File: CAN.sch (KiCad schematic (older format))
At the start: 7 parts, among them IC1 ADM3052

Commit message: - updated project to 5.0.0 - added ignore file
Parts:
- C10, C11, C12, C9: symbol C_Small -> Device:C_Small
- IC1: symbol ADM3052 -> HSWR-V2-rescue:ADM3052
- R30, R31: symbol R_Small -> Device:R_Small
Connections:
- wire segments 4 -> 2
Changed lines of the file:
@@
-EESchema Schematic File Version 2
-LIBS:HSWR V2-rescue
-LIBS:power
-LIBS:device
-LIBS:transistors
-LIBS:conn
-LIBS:linear
-LIBS:regul
-LIBS:74xx
-LIBS:cmos4000
-LIBS:adc-dac
-LIBS:memory
-LIBS:xilinx
-LIBS:microcontrollers
-LIBS:dsp
-LIBS:microchip
-LIBS:analog_switches
-LIBS:motorola
-LIBS:texas
-LIBS:intel
-LIBS:audio
-LIBS:interface
-LIBS:digital-audio
-LIBS:philips
-LIBS:display
-LIBS:cypress
-LIBS:siliconi
-LIBS:opto
-LIBS:atmel
-LIBS:contrib
-LIBS:valves
+EESchema Schematic File Version 4
 LIBS:HSWR V2-cache
-EELAYER 25 0
+EELAYER 26 0
 EELAYER END
 $Descr A4 11693 8268
@@
 CANL
 $Comp
-L ADM3052 IC1
+L HSWR-V2-rescue:ADM3052 IC1
 U 1 1 5759CEA3
 P 6000 3850
+AR Path="/5759CEA3" Ref="IC1"  Part="1"
+AR Path="/5899E225/5759CEA3" Ref="IC1"  Part="1"
 F 0 "IC1" H 6000 3850 60  0000 C CNN
 F 1 "ADM3052" H 6000 4500 60  0000 C CNN
@@
 $EndComp
 $Comp
-L C_Small C9
+L Device:C_Small C9
 U 1 1 5759CF39
 P 5350 3900
@@
 $EndComp
 $Comp
-L C_Small C10
+L Device:C_Small C10
 U 1 1 5759CF9E
 P 5350 4200
@@
 Connection ~ 5350 4300
 $Comp
-L R_Small R31
+L Device:R_Small R31
 U 1 1 5759CFE0
 P 5350 4400
@@
 $EndComp
 $Comp
-L C_Small C11
+L Device:C_Small C11
 U 1 1 5759D08A
 P 5350 4600
@@
 Connection ~ 5350 4500
 $Comp
-L Earth #PWR029
+L power:Earth #PWR029
 U 1 1 5759DCFE
 P 5350 4700
@@
 $EndComp
 $Comp
-L Earth #PWR030
+L power:Earth #PWR030
 U 1 1 5759DF52
 P 5350 4100
@@
 $EndComp
 $Comp
-L +12VA #PWR031
+L power:+12VA #PWR031
 U 1 1 5759E22F
 P 5350 4500
@@
 $EndComp
 $Comp
-L GND #PWR032
+L power:GND #PWR032
 U 1 1 5759E8F5
 P 6650 4500
@@
 $EndComp
 $Comp
-L R_Small R30
+L Device:R_Small R30
 U 1 1 5759ED7A
 P 5350 3250
@@
 V+Sense
 $Comp
-L C_Small C12
+L Device:C_Small C12
 U 1 1 575A0498
 P 6650 4200
@@
 Connection ~ 6650 4500
 $Comp
-L +3V3 #PWR033
+L power:+3V3 #PWR033
 U 1 1 575A0BC8
 P 6650 4100
@@
 	1    0    0    -1
 $EndComp
-Wire Wire Line
-	6650 4300 6650 4500
 Connection ~ 6650 4400
-Wire Wire Line
-	5350 4000 5350 4100
 Connection ~ 5350 4000
 Connection ~ 6650 4100

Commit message: - updated to VESC6 architecture - still some things to do in schematic
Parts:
- removed IC1: ADM3052, Housings_SOIC:SOIC-16_7.5x10.3mm_Pitch1.27mm, symbol HSWR-V2-rescue:ADM3052
- C10, C11, C12, C9: footprint Capacitors_SMD:C_0805 -> Capacitor_SMD:C_0805_2012Metric
- R30: footprint Resistors_SMD:R_0805 -> Resistor_SMD:R_0805_2012Metric
- R31: footprint Resistors_SMD:R_1206 -> Resistor_SMD:R_0805_2012Metric
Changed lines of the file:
@@
 $Descr A4 11693 8268
 encoding utf-8
-Sheet 3 7
+Sheet 2 7
 Title "HSWR CAN Transceiver"
 Date "2017-02-05"
@@
 CANL
 $Comp
-L HSWR-V2-rescue:ADM3052 IC1
-U 1 1 5759CEA3
-P 6000 3850
-AR Path="/5759CEA3" Ref="IC1"  Part="1"
-AR Path="/5899E225/5759CEA3" Ref="IC1"  Part="1"
-F 0 "IC1" H 6000 3850 60  0000 C CNN
-F 1 "ADM3052" H 6000 4500 60  0000 C CNN
-F 2 "Housings_SOIC:SOIC-16_7.5x10.3mm_Pitch1.27mm" H 6150 3950 60  0001 C CNN
-F 3 "" H 6150 3950 60  0000 C CNN
-	1    6000 3850
-	-1   0    0    -1
-$EndComp
-$Comp
 L Device:C_Small C9
 U 1 1 5759CF39
@@
 F 0 "C9" H 5500 4000 50  0000 L CNN
 F 1 "1u" H 5500 3900 50  0000 L CNN
-F 2 "Capacitors_SMD:C_0805" H 5350 3900 60  0001 C CNN
+F 2 "Capacitor_SMD:C_0805_2012Metric" H 5350 3900 60  0001 C CNN
 F 3 "" H 5350 3900 60  0000 C CNN
 	1    5350 3900
@@
 F 0 "C10" H 5450 4250 50  0000 L CNN
 F 1 "10u" H 5450 4150 50  0000 L CNN
-F 2 "Capacitors_SMD:C_0805" H 5350 4200 60  0001 C CNN
+F 2 "Capacitor_SMD:C_0805_2012Metric" H 5350 4200 60  0001 C CNN
 F 3 "" H 5350 4200 60  0000 C CNN
 	1    5350 4200
 	-1   0    0    -1
 $EndComp
-Connection ~ 5350 4100
-Connection ~ 5350 4300
 $Comp
 L Device:R_Small R31
@@
 F 0 "R31" V 5250 4350 50  0000 L CNN
 F 1 "300R" H 5400 4400 50  0000 L CNN
-F 2 "Resistors_SMD:R_1206" H 5350 4400 60  0001 C CNN
+F 2 "Resistor_SMD:R_0805_2012Metric" H 5350 4400 60  0001 C CNN
 F 3 "" H 5350 4400 60  0000 C CNN
 	1    5350 4400
@@
 F 0 "C11" H 5500 4600 50  0000 L CNN
 F 1 "100n" H 5450 4500 50  0000 L CNN
-F 2 "Capacitors_SMD:C_0805" H 5350 4600 60  0001 C CNN
+F 2 "Capacitor_SMD:C_0805_2012Metric" H 5350 4600 60  0001 C CNN
 F 3 "" H 5350 4600 60  0000 C CNN
 	1    5350 4600
@@
 F 0 "R30" V 5250 3200 50  0000 L CNN
 F 1 "120R" H 5400 3250 50  0000 L CNN
-F 2 "Resistors_SMD:R_0805" H 5350 3250 60  0001 C CNN
+F 2 "Resistor_SMD:R_0805_2012Metric" H 5350 3250 60  0001 C CNN
 F 3 "" H 5350 3250 60  0000 C CNN
 	1    5350 3250
@@
 Wire Wire Line
 	5350 3150 5150 3150
-Connection ~ 5350 3150
-Connection ~ 5350 3350
 Text HLabel 6650 3550 2    60   Output ~ 0
 V+Sense
@@
 F 0 "C12" H 6800 4200 50  0000 L CNN
 F 1 "100n" H 6750 4100 50  0000 L CNN
-F 2 "Capacitors_SMD:C_0805" H 6650 4200 60  0001 C CNN
+F 2 "Capacitor_SMD:C_0805_2012Metric" H 6650 4200 60  0001 C CNN
 F 3 "" H 6650 4200 60  0000 C CNN
 	1    6650 4200
 	1    0    0    -1
 $EndComp
-Connection ~ 6650 4300
-Connection ~ 6650 4500
 $Comp
 L power:+3V3 #PWR033
@@
 	1    0    0    -1
 $EndComp
-Connection ~ 6650 4400
-Connection ~ 5350 4000
-Connection ~ 6650 4100
 $EndSCHEMATC

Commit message: - layout pretty much finished except PSU and maaaaybe R2D - started work on R2D with AD2S1205
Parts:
- removed C10: 10u, Capacitor_SMD:C_0805_2012Metric, symbol Device:C_Small
- removed R31: 300R, Resistor_SMD:R_0805_2012Metric, symbol Device:R_Small
- added IC4: ADUM3054, Package_SO:SOIC-16W_7.5x10.3mm_P1.27mm, symbol Auktoralib:ADUM3054
- added U5: AP1117-50, Package_TO_SOT_SMD:SOT-223-3_TabPin2, symbol Regulator_Linear:AP1117-50
- C9: value 1u -> 100n
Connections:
- net labels added: 12V_ext
- net labels removed: +12VA
- wire segments 2 -> 8
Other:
- moved on the sheet: C11, C12, C9
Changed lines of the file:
@@
 $Descr A4 11693 8268
 encoding utf-8
-Sheet 2 7
+Sheet 7 9
 Title "HSWR CAN Transceiver"
 Date "2017-02-05"
@@
 Comment4 ""
 $EndDescr
-Text HLabel 6650 3350 2    60   Output ~ 0
+Text HLabel 6550 3400 2    60   Output ~ 0
 CAN_RX
-Text HLabel 6650 3150 2    60   Input ~ 0
+Text HLabel 6550 3500 2    60   Input ~ 0
 CAN_TX
 Text HLabel 5150 3150 0    60   Input ~ 0
@@
 L Device:C_Small C9
 U 1 1 5759CF39
-P 5350 3900
-F 0 "C9" H 5500 4000 50  0000 L CNN
-F 1 "1u" H 5500 3900 50  0000 L CNN
-F 2 "Capacitor_SMD:C_0805_2012Metric" H 5350 3900 60  0001 C CNN
-F 3 "" H 5350 3900 60  0000 C CNN
-	1    5350 3900
-	-1   0    0    -1
-$EndComp
-$Comp
-L Device:C_Small C10
-U 1 1 5759CF9E
-P 5350 4200
-F 0 "C10" H 5450 4250 50  0000 L CNN
-F 1 "10u" H 5450 4150 50  0000 L CNN
-F 2 "Capacitor_SMD:C_0805_2012Metric" H 5350 4200 60  0001 C CNN
-F 3 "" H 5350 4200 60  0000 C CNN
-	1    5350 4200
-	-1   0    0    -1
-$EndComp
-$Comp
-L Device:R_Small R31
-U 1 1 5759CFE0
-P 5350 4400
-F 0 "R31" V 5250 4350 50  0000 L CNN
-F 1 "300R" H 5400 4400 50  0000 L CNN
-F 2 "Resistor_SMD:R_0805_2012Metric" H 5350 4400 60  0001 C CNN
-F 3 "" H 5350 4400 60  0000 C CNN
-	1    5350 4400
+P 5700 2600
+F 0 "C9" H 5800 2600 50  0000 L CNN
+F 1 "100n" H 5750 2500 50  0000 L CNN
+F 2 "Capacitor_SMD:C_0805_2012Metric" H 5700 2600 60  0001 C CNN
+F 3 "" H 5700 2600 60  0000 C CNN
+	1    5700 2600
 	-1   0    0    -1
 $EndComp
@@
 L Device:C_Small C11
 U 1 1 5759D08A
-P 5350 4600
-F 0 "C11" H 5500 4600 50  0000 L CNN
-F 1 "100n" H 5450 4500 50  0000 L CNN
-F 2 "Capacitor_SMD:C_0805_2012Metric" H 5350 4600 60  0001 C CNN
-F 3 "" H 5350 4600 60  0000 C CNN
-	1    5350 4600
-	-1   0    0    -1
-$EndComp
-Connection ~ 5350 4500
+P 4350 2600
+F 0 "C11" H 4500 2600 50  0000 L CNN
+F 1 "100n" H 4450 2500 50  0000 L CNN
+F 2 "Capacitor_SMD:C_0805_2012Metric" H 4350 2600 60  0001 C CNN
+F 3 "" H 4350 2600 60  0000 C CNN
+	1    4350 2600
+	-1   0    0    -1
+$EndComp
 $Comp
 L power:Earth #PWR029
 U 1 1 5759DCFE
-P 5350 4700
-F 0 "#PWR029" H 5350 4450 50  0001 C CNN
-F 1 "Earth" H 5350 4550 50  0001 C CNN
-F 2 "" H 5350 4700 60  0000 C CNN
-F 3 "" H 5350 4700 60  0000 C CNN
-	1    5350 4700
-	-1   0    0    -1
-$EndComp
-$Comp
-L power:Earth #PWR030
-U 1 1 5759DF52
-P 5350 4100
-F 0 "#PWR030" H 5350 3850 50  0001 C CNN
-F 1 "Earth" H 5350 3950 50  0001 C CNN
-F 2 "" H 5350 4100 60  0000 C CNN
-F 3 "" H 5350 4100 60  0000 C CNN
-	1    5350 4100
-	0    1    -1   0
-$EndComp
-$Comp
-L power:+12VA #PWR031
-U 1 1 5759E22F
-P 5350 4500
-F 0 "#PWR031" H 5350 4350 50  0001 C CNN
-F 1 "+12VA" V 5350 4750 50  0000 C CNN
-F 2 "" H 5350 4500 60  0000 C CNN
-F 3 "" H 5350 4500 60  0000 C CNN
-	1    5350 4500
-	0    -1   -1   0
+P 4650 2800
+F 0 "#PWR029" H 4650 2550 50  0001 C CNN
+F 1 "Earth" H 4650 2650 50  0001 C CNN
+F 2 "" H 4650 2800 60  0000 C CNN
+F 3 "" H 4650 2800 60  0000 C CNN
+	1    4650 2800
+	-1   0    0    -1
 $EndComp
 $Comp
 L power:GND #PWR032
 U 1 1 5759E8F5
-P 6650 4500
-F 0 "#PWR032" H 6650 4250 50  0001 C CNN
-F 1 "GND" H 6650 4350 50  0000 C CNN
-F 2 "" H 6650 4500 60  0000 C CNN
-F 3 "" H 6650 4500 60  0000 C CNN
-	1    6650 4500
+P 6050 4050
+F 0 "#PWR032" H 6050 3800 50  0001 C CNN
+F 1 "GND" H 6050 3900 50  0000 C CNN
+F 2 "" H 6050 4050 60  0000 C CNN
+F 3 "" H 6050 4050 60  0000 C CNN
+	1    6050 4050
 	1    0    0    -1
 $EndComp
@@
 Wire Wire Line
 	5350 3150 5150 3150
-Text HLabel 6650 3550 2    60   Output ~ 0
+Text HLabel 6550 3300 2    60   Output ~ 0
 V+Sense
 $Comp
 L Device:C_Small C12
 U 1 1 575A0498
-P 6650 4200
-F 0 "C12" H 6800 4200 50  0000 L CNN
-F 1 "100n" H 6750 4100 50  0000 L CNN
-F 2 "Capacitor_SMD:C_0805_2012Metric" H 6650 4200 60  0001 C CNN
-F 3 "" H 6650 4200 60  0000 C CNN
-	1    6650 4200
+P 6200 2600
+F 0 "C12" H 6350 2600 50  0000 L CNN
+F 1 "100n" H 6300 2500 50  0000 L CNN
+F 2 "Capacitor_SMD:C_0805_2012Metric" H 6200 2600 60  0001 C CNN
+F 3 "" H 6200 2600 60  0000 C CNN
+	1    6200 2600
 	1    0    0    -1
 $EndComp
@@
 L power:+3V3 #PWR033
 U 1 1 575A0BC8
-P 6650 4100
-F 0 "#PWR033" H 6650 3950 50  0001 C CNN
-F 1 "+3V3" H 6650 4240 50  0000 C CNN
-F 2 "" H 6650 4100 60  0000 C CNN
-F 3 "" H 6650 4100 60  0000 C CNN
-	1    6650 4100
-	1    0    0    -1
-$EndComp
+P 6200 2500
+F 0 "#PWR033" H 6200 2350 50  0001 C CNN
+F 1 "+3V3" H 6200 2640 50  0000 C CNN
+F 2 "" H 6200 2500 60  0000 C CNN
+F 3 "" H 6200 2500 60  0000 C CNN
+	1    6200 2500
+	1    0    0    -1
+$EndComp
+$Comp
+L power:Earth #PWR0115
+U 1 1 5CA085F6
+P 5700 2700
+F 0 "#PWR0115" H 5700 2450 50  0001 C CNN
+F 1 "Earth" H 5700 2550 50  0001 C CNN
+F 2 "" H 5700 2700 60  0000 C CNN
+F 3 "" H 5700 2700 60  0000 C CNN
+	1    5700 2700
+	-1   0    0    -1
+$EndComp
+Text HLabel 4350 2500 0    50   Input ~ 0
+12V_ext
+$Comp
+L Regulator_Linear:AP1117-50 U5
+U 1 1 5CA08F00
+P 4650 2500
+F 0 "U5" H 4650 2742 50  0000 C CNN
+F 1 "AP1117-50" H 4650 2651 50  0000 C CNN
+F 2 "Package_TO_SOT_SMD:SOT-223-3_TabPin2" H 4650 2700 50  0001 C CNN
+F 3 "http://www.diodes.com/datasheets/AP1117.pdf" H 4750 2250 50  0001 C CNN
+	1    4650 2500
+	1    0    0    -1
+$EndComp
+$Comp
+L power:Earth #PWR0167
+U 1 1 5CA09500
+P 4350 2800
+F 0 "#PWR0167" H 4350 2550 50  0001 C CNN
+F 1 "Earth" H 4350 2650 50  0001 C CNN
+F 2 "" H 4350 2800 60  0000 C CNN
+F 3 "" H 4350 2800 60  0000 C CNN
+	1    4350 2800
+	-1   0    0    -1
+$EndComp
+Wire Wire Line
+	4350 2800 4350 2700
+Wire Wire Line
+	4950 2500 5700 2500
+Wire Wire Line
+	5850 2500 5850 2750
+Connection ~ 5700 2500
+Wire Wire Line
+	5700 2500 5850 2500
+Connection ~ 5350 3150
+Connection ~ 5350 3350
+$Comp
+L Auktoralib:ADUM3054 IC4
+U 1 1 5CA06D6C
+P 5950 3400
+F 0 "IC4" H 5500 2850 50  0000 C CNN
+F 1 "ADUM3054" H 6350 3900 50  0000 C CNN
+F 2 "Package_SO:SOIC-16W_7.5x10.3mm_P1.27mm" H 5950 3300 50  0001 C CNN
+F 3 "" H 5950 3300 50  0001 C CNN
+	1    5950 3400
+	-1   0    0    -1
+$EndComp
+$Comp
+L power:Earth #PWR0168
+U 1 1 5CA09CBC
+P 5750 4050
+F 0 "#PWR0168" H 5750 3800 50  0001 C CNN
+F 1 "Earth" H 5750 3900 50  0001 C CNN
+F 2 "" H 5750 4050 60  0000 C CNN
+F 3 "" H 5750 4050 60  0000 C CNN
+	1    5750 4050
+	-1   0    0    -1
+$EndComp
+$Comp
+L power:Earth #PWR0169
+U 1 1 5CA09D7B
+P 5850 4050
+F 0 "#PWR0169" H 5850 3800 50  0001 C CNN
+F 1 "Earth" H 5850 3900 50  0001 C CNN
+F 2 "" H 5850 4050 60  0000 C CNN
+F 3 "" H 5850 4050 60  0000 C CNN
+	1    5850 4050
+	-1   0    0    -1
+$EndComp
+$Comp
+L power:GND #PWR0170
+U 1 1 5CA0A130
+P 6150 4050
+F 0 "#PWR0170" H 6150 3800 50  0001 C CNN
+F 1 "GND" H 6150 3850 50  0000 C CNN
+F 2 "" H 6150 4050 60  0000 C CNN
+F 3 "" H 6150 4050 60  0000 C CNN
+	1    6150 4050
+	1    0    0    -1
+$EndComp
+$Comp
+L power:GND #PWR0171
+U 1 1 5CA0A147
+P 6250 4050
+F 0 "#PWR0171" H 6250 3800 50  0001 C CNN
+F 1 "GND" H 6250 3900 50  0000 C CNN
+F 2 "" H 6250 4050 60  0000 C CNN
+F 3 "" H 6250 4050 60  0000 C CNN
+	1    6250 4050
+	1    0    0    -1
+$EndComp
+$Comp
+L power:GND #PWR0172
+U 1 1 5CA0A1E2
+P 6200 2700
+F 0 "#PWR0172" H 6200 2450 50  0001 C CNN
+F 1 "GND" H 6200 2550 50  0000 C CNN
+F 2 "" H 6200 2700 60  0000 C CNN
+F 3 "" H 6200 2700 60  0000 C CNN
+	1    6200 2700
+	1    0    0    -1
+$EndComp
+Wire Wire Line
+	6050 2750 6050 2500
+Wire Wire Line
+	6050 2500 6200 2500
+Connection ~ 6200 2500
 $EndSCHEMATC

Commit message: - removed R2D.sch - selected PSUs - finished layout
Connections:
- net labels added: +12VA
- net labels removed: 12V_ext
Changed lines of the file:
@@
 $Descr A4 11693 8268
 encoding utf-8
-Sheet 7 9
+Sheet 7 8
 Title "HSWR CAN Transceiver"
 Date "2017-02-05"
@@
 	-1   0    0    -1
 $EndComp
-Text HLabel 4350 2500 0    50   Input ~ 0
-12V_ext
 $Comp
 L Regulator_Linear:AP1117-50 U5
@@
 	6050 2500 6200 2500
 Connection ~ 6200 2500
+$Comp
+L power:+12VA #PWR0199
+U 1 1 5C9EF966
+P 4350 2500
+F 0 "#PWR0199" H 4350 2350 50  0001 C CNN
+F 1 "+12VA" H 4365 2673 50  0000 C CNN
+F 2 "" H 4350 2500 50  0001 C CNN
+F 3 "" H 4350 2500 50  0001 C CNN
+	1    4350 2500
+	1    0    0    -1
+$EndComp
+Connection ~ 4350 2500
 $EndSCHEMATC

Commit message: - corrected current filter resistors - adapted USB footprint - added 0.1% note to dc bus voltage divider
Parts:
- IC4: symbol Auktoralib:ADUM3054 -> HSWR-V2-rescue:ADUM3054-Auktoralib
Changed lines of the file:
@@
 Connection ~ 5350 3350
 $Comp
-L Auktoralib:ADUM3054 IC4
+L HSWR-V2-rescue:ADUM3054-Auktoralib IC4
 U 1 1 5CA06D6C
 P 5950 3400
+AR Path="/5CA06D6C" Ref="IC4"  Part="1"
+AR Path="/5899E225/5CA06D6C" Ref="IC4"  Part="1"
 F 0 "IC4" H 5500 2850 50  0000 C CNN
 F 1 "ADUM3054" H 6350 3900 50  0000 C CNN

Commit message: first commit of Amalga_100.
R2D needs to be finished.
Logicpart needs to be routed.
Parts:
- removed IC4: ADUM3054, Package_SO:SOIC-16W_7.5x10.3mm_P1.27mm, symbol HSWR-V2-rescue:ADUM3054-Auktoralib
- removed U5: AP1117-50, Package_TO_SOT_SMD:SOT-223-3_TabPin2, symbol Regulator_Linear:AP1117-50
- added C10: 10u, Capacitor_SMD:C_0805_2012Metric, symbol Amalga_100-rescue:C_Small-Device
- added IC1: ADM3052, Package_SO:SOIC-16W_7.5x10.3mm_P1.27mm, symbol Amalga_100-rescue:ADM3052-HSWR-V2-rescue
- added R31: 300R, Resistor_SMD:R_1206_3216Metric, symbol Amalga_100-rescue:R_Small-Device
- C11, C12: symbol Device:C_Small -> Amalga_100-rescue:C_Small-Device
- C9: value 100n -> 1u; symbol Device:C_Small -> Amalga_100-rescue:C_Small-Device
- R30: symbol Device:R_Small -> Amalga_100-rescue:R_Small-Device
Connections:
- net +12VA: now also IC1.15 (V+), R31.2
- net +3V3: now also IC1.7 (VDD1)
- net CANH: now also IC1.12 (CANH)
- net CANL: now also IC1.11 (CANL)
- net CAN_RX: now also IC1.5 (RxD)
- net CAN_TX: now also IC1.6 (TxD)
- net Earth: now also C10.1, IC1.9 (V-); no longer C9.2
- net GND: now also IC1.8 (GND1); no longer C12.2
- net V+Sense: now also IC1.4 (V+Sense)
- net at C9.1: now also IC1.13 (Cint)
- new net: C10.2, IC1.14 (V+R), R31.1
- new net: C9.2, IC1.16 (V-)
- new net: C12.2, IC1.2 (GND1)
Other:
- moved on the sheet: C11, C12, C9

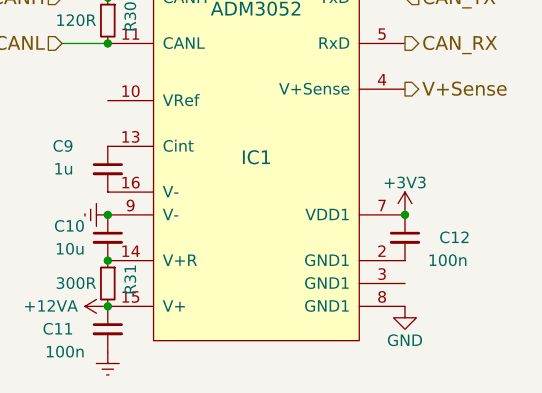
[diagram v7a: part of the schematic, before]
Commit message: continued Resolver continued Routing
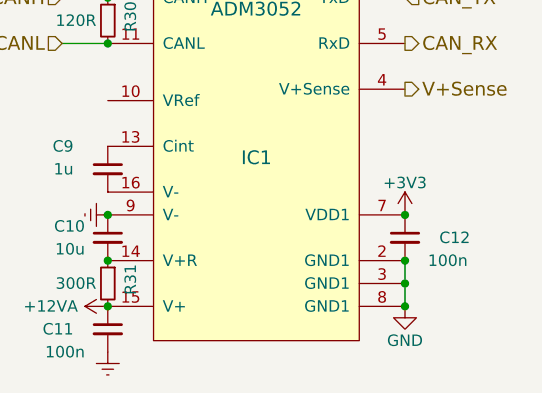
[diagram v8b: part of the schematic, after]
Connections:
- net GND: now also C12.2, IC1.2 (GND1), IC1.3 (GND1)
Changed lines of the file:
@@
 $EndComp
 Connection ~ 6650 4100
+Wire Wire Line
+	6650 4300 6650 4400
+Connection ~ 6650 4300
+Connection ~ 6650 4500
+Connection ~ 6650 4400
+Wire Wire Line
+	6650 4400 6650 4500
 $EndSCHEMATC
